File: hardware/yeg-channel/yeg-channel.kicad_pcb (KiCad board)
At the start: 2 copper layers, 74.9 x 51.4 mm, 106 parts, among them J1 Conn_ADC, J2 Conn_Debug, J3 Conn_SPI_Input, J4 Conn_SPI_Output, SW1 SW_RST, SW2 SW_BOOT0, SW3 SW_BOOT1, U1 AMS1117-3.3, U10 HX71708, U11 74HC4051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

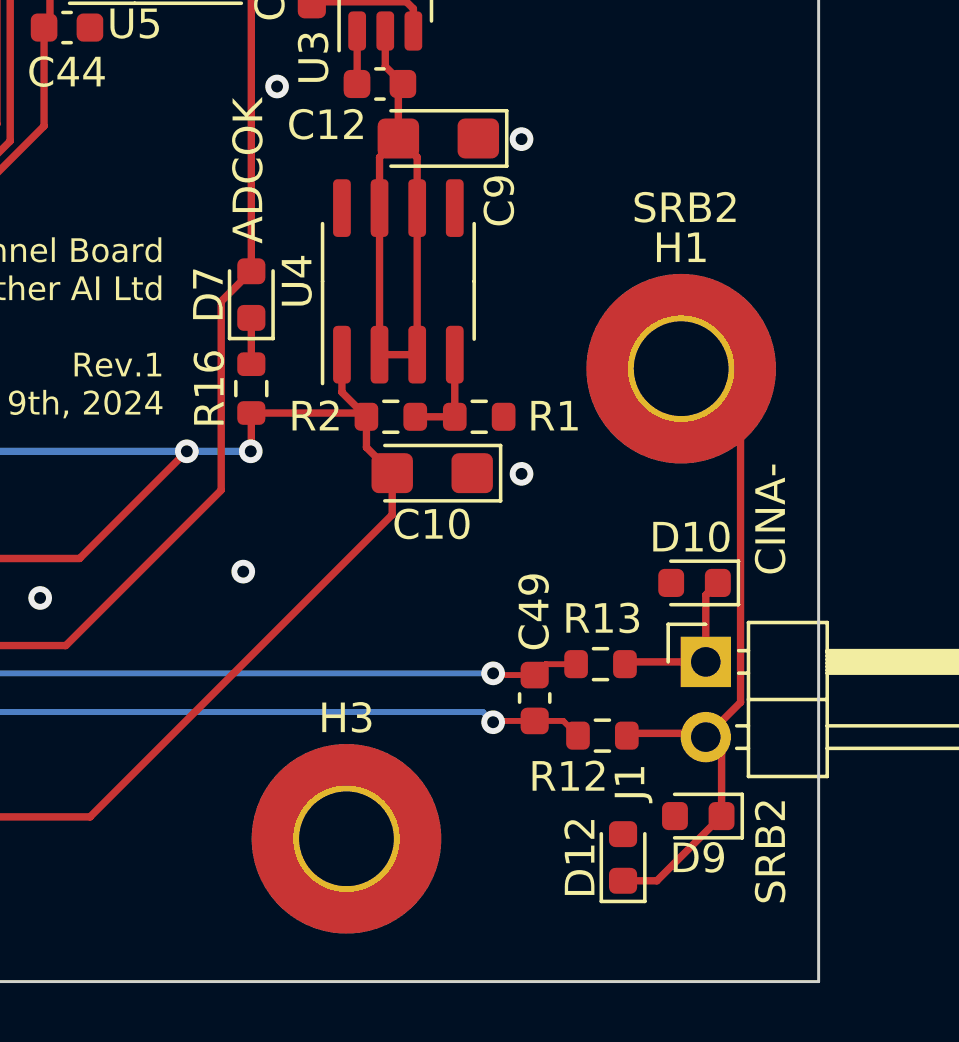
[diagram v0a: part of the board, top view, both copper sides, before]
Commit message: move srb2 to a closer port
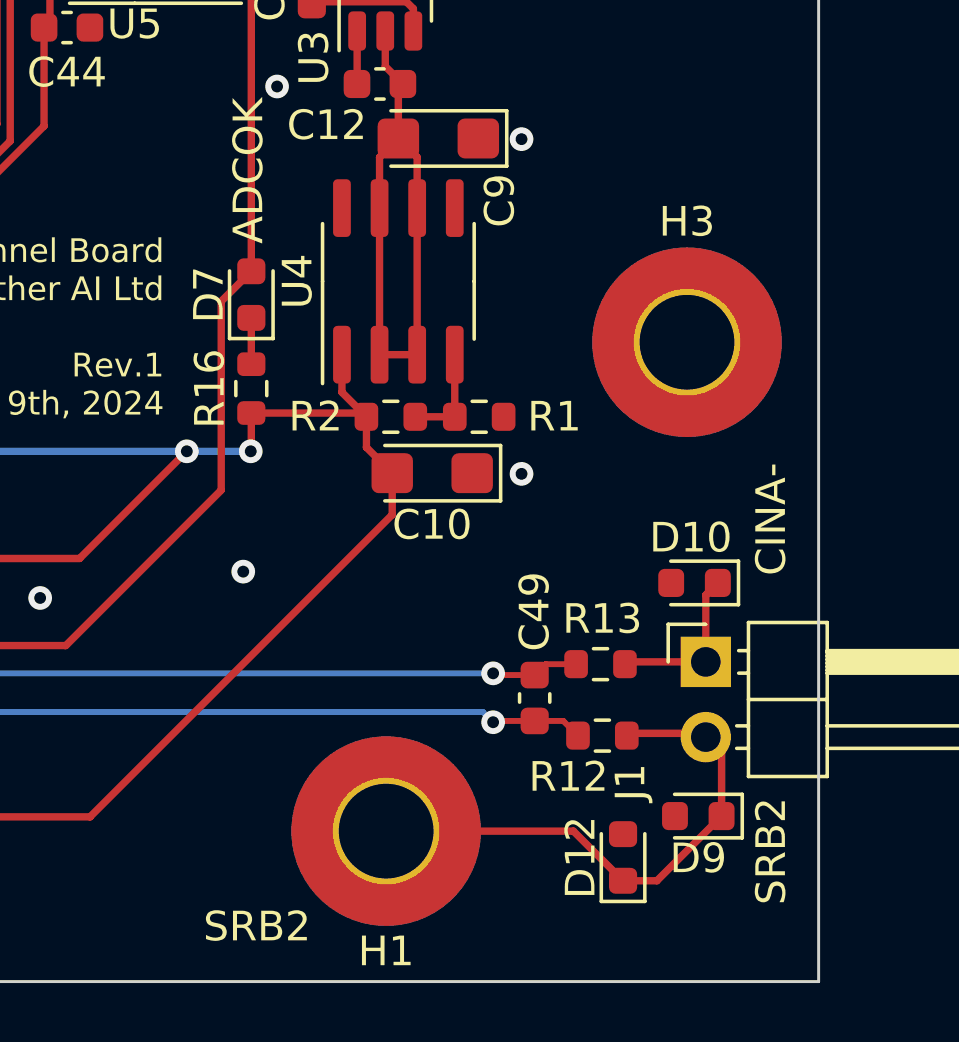
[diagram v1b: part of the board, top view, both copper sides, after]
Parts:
- moved H3 20.3 mm to (127.6, 66.0)
- moved H1 18.5 mm to (117.5, 82.5), turned to 0 degrees
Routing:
- net /ADC/SRB2: track 23.4 -> 18.3 mm
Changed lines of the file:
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@@
   )
   (footprint "MountingHole:MountingHole_3.2mm_M3_Pad_TopBottom" (layer "F.Cu")
-    (at 127.438 66.934 180)
+    (at 117.475 82.55)
     (descr "Mounting Hole 3.2mm, M3")
     (tags "mounting hole 3.2mm m3")
@@
     (fp_circle (center 0 0) (end 3.45 0)
       (stroke (width 0.05) (type solid)) (fill none) (layer "F.CrtYd"))
-    (pad "1" thru_hole circle (at 0 0 180) (size 3.6 3.6) (drill 3.2) (layers "*.Cu" "*.Mask")
+    (pad "1" thru_hole circle (at 0 0) (size 3.6 3.6) (drill 3.2) (layers "*.Cu" "*.Mask")
       (net 29 "/ADC/SRB2") (pinfunction "1") (pintype "input"))
-    (pad "1" connect circle (at 0 0 180) (size 6.4 6.4) (layers "F.Cu" "F.Mask")
+    (pad "1" connect circle (at 0 0) (size 6.4 6.4) (layers "F.Cu" "F.Mask")
       (net 29 "/ADC/SRB2") (pinfunction "1") (pintype "input"))
-    (pad "1" connect circle (at 0 0 180) (size 6.4 6.4) (layers "B.Cu" "B.Mask")
+    (pad "1" connect circle (at 0 0) (size 6.4 6.4) (layers "B.Cu" "B.Mask")
       (net 29 "/ADC/SRB2") (pinfunction "1") (pintype "input"))
   )
@@
   )
   (footprint "MountingHole:MountingHole_3.2mm_M3_Pad_TopBottom" (layer "F.Cu")
-    (at 116.135 82.809)
+    (at 127.635 66.04)
     (descr "Mounting Hole 3.2mm, M3")
     (tags "mounting hole 3.2mm m3")
@@
     (effects (font (size 1 1) (thickness 0.15)) (justify right bottom))
   )
-  (gr_text "SRB2" (at 129.413 62.103) (layer "F.SilkS")
+  (gr_text "SRB2" (at 114.935 86.36) (layer "F.SilkS")
     (effects (font (size 1 1) (thickness 0.15)) (justify right bottom))
   )
@@
   (segment (start 86.030052 53.754552) (end 86.030052 56.919552) (width 0.25) (layer "F.Cu") (net 28))
   (segment (start 86.030052 56.919552) (end 92.525552 63.415052) (width 0.25) (layer "F.Cu") (net 28))
-  (segment (start 129.445 68.941) (end 129.445 78.2) (width 0.25) (layer "F.Cu") (net 29))
   (segment (start 128.8035 82.042) (end 128.8035 79.9085) (width 0.25) (layer "F.Cu") (net 29))
   (segment (start 128.143 79.248) (end 128.27 79.375) (width 0.25) (layer "F.Cu") (net 29))
   (segment (start 125.793 79.248) (end 128.143 79.248) (width 0.25) (layer "F.Cu") (net 29))
-  (segment (start 127.438 66.934) (end 129.445 68.941) (width 0.25) (layer "F.Cu") (net 29))
+  (segment (start 117.475 82.55) (end 123.7995 82.55) (width 0.25) (layer "F.Cu") (net 29))
+  (segment (start 123.7995 82.55) (end 125.476 84.2265) (width 0.25) (layer "F.Cu") (net 29))
   (segment (start 126.619 84.2265) (end 128.8035 82.042) (width 0.25) (layer "F.Cu") (net 29))
   (segment (start 125.476 84.2265) (end 126.619 84.2265) (width 0.25) (layer "F.Cu") (net 29))
   (segment (start 128.8035 79.9085) (end 128.27 79.375) (width 0.25) (layer "F.Cu") (net 29))
-  (segment (start 129.445 78.2) (end 128.27 79.375) (width 0.25) (layer "F.Cu") (net 29))
   (segment (start 128.27 74.5745) (end 128.6765 74.168) (width 0.25) (layer "F.Cu") (net 30))
   (segment (start 128.27 76.835) (end 128.27 74.5745) (width 0.25) (layer "F.Cu") (net 30))
